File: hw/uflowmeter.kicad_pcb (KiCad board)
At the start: 4 copper layers, 70 x 55 mm, 54 parts, among them J1 SBW, J2 ANT, J3 Display, J4 Transducers, J5 Cal UART, Q1 IRLML6401, SW1 Button, U1 MSP430FR5043IRGC, U2 CC1101RGPR, Y1 32.768kHz, Y2 8MHz, Y3 26MHz

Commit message: hw: fabrication export, fiducials, and an honest account of what is left
make_fab.sh writes the JLCPCB set from the board file: the four copper
layers, both masks, silkscreens and paste layers, the outline and both drill
files, zipped, plus the BOM and the placement CSV in the column names the
assembly step wants. It caught its own bug on the first run -- KiCad names
Gerbers by layer, .gtl .gbl .g1 .g2 and so on, so a wildcard on .gbr ships an
archive containing nothing but drill files.

finish_board.py adds what a router will not: three fiducials in an asymmetric
L, because a QFN-64 on 0.5 mm pitch is placed from fiducials rather than from
the board outline, and a legend on both sides.

The board is NOT orderable, and the docs now say so plainly. 32 connections
are missing. Fifteen are the RF chain: route_rf.py manages two hops of
eighteen because the shunt parts sit across the straight line between the
series ones, and making room means choosing a geometry, which is the one
thing that must not be chosen freely -- TI's values are only correct with
TI's layout. That layout is in the SWRR045 archive as CADSTAR and Gerbers,
readable by a person and not by a script.

The other seventeen are signals on fifteen nets, almost all the last pins of
the two QFNs where the room runs out. They want a router that can push what
is already laid; mine only add.

Three dead ends are recorded so nobody repeats them: reordering the nets (six
orderings, the one in use was best, and hardest-first scored worst),
unbounding the search (12 mm to 30 mm margin changed the result by exactly
nothing), and running further passes (identical output plus duplicate
copper). What is left is congestion, and congestion wants rip-up.

Co-Authored-By: Claude Opus 5 (1M context) <noreply@anthropic.com>
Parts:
- added FID1: , Fiducial_1mm_Mask2mm, F.Cu at (3.45, 3.45)
- added FID2: , Fiducial_1mm_Mask2mm, F.Cu at (66.5, 3.45)
- added FID3: , Fiducial_1mm_Mask2mm, F.Cu at (3.45, 51.5)
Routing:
- net RFE: track 0.00 -> 4.00 mm
- net RFC: track 0.00 -> 3.00 mm
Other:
- board text added: "uflowmeter rev A"

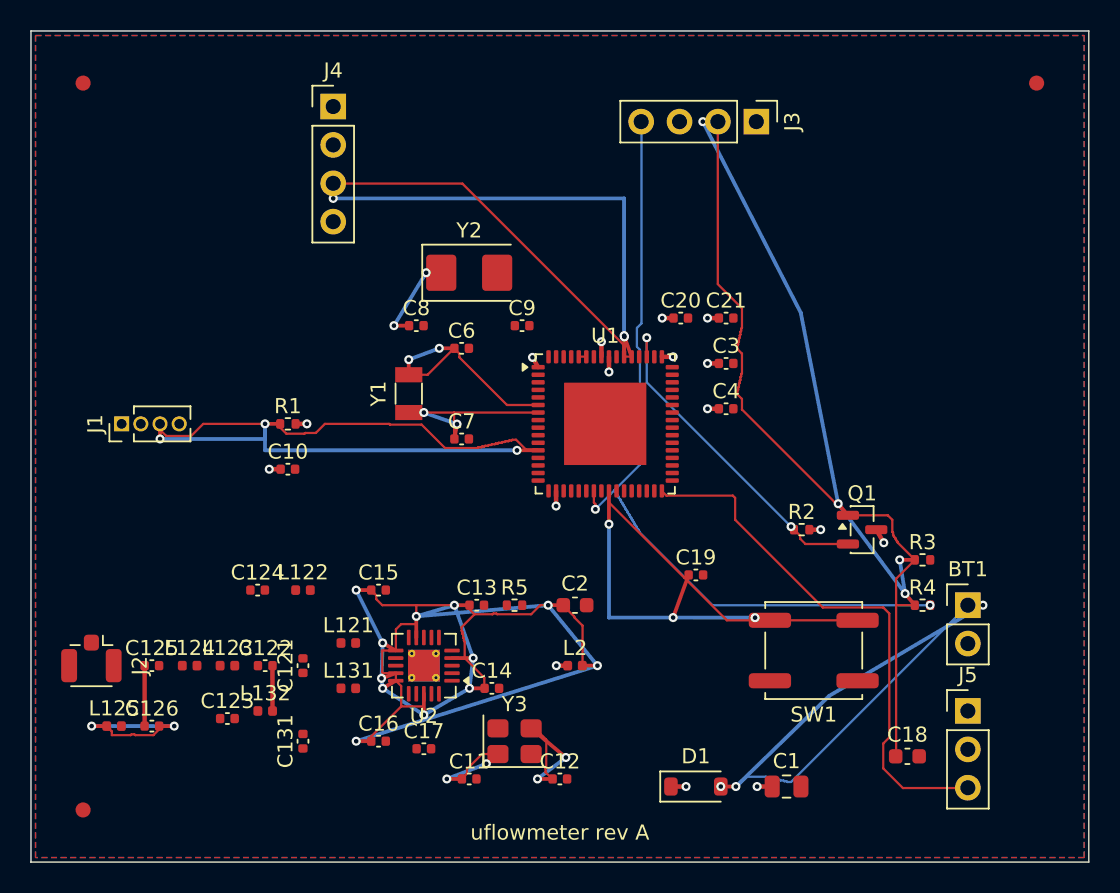
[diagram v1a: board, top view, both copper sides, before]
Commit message: hw: the radio becomes a module, and a real schematic that caught a real bug
The CC1101 is no longer on this board. Gone with it: its 26 MHz crystal, its
bias resistor, its supply bead and decoupling, the whole filter balun and the
notch, and the u.FL connector -- twenty parts. J6 carries eight pins to a
ready-made module instead, and the firmware did not change by a line.

That removed the two hardest problems in the design. TI's reference layout no
longer has to be transplanted, which mattered because it exists only as
CADSTAR and Gerbers -- readable by a person, not by a script. And EN 300 220
no longer has to be proven by conducted measurement, which an antenna
connector on your own board obliges you to do.

What the module must be is now in RF.md, and the third condition is the one
that quietly ruins a battery meter: no power LED. An indicator LED is a
milliamp against this instrument's 5.7 uA, two hundred times the whole thing.

uflowmeter.kicad_sch is generated from the netlist with every symbol drawn in
the file, so it opens the same anywhere. It is verified the only way that
proves anything: export the netlist back out of it and compare. The first run
disagreed on RST -- and it was not the generator that was wrong. C10 pin 1 was
declared on both VCC and RST. It is the reset capacitor; its plate belongs to
RST alone. mknet.py now refuses to emit a netlist where two nets claim one
pad.

The board that comes out of all this is 29 components and 22 nets, down from
54 and 37. Routing went from 34 unconnected to 6, DRC clean. build_board.sh
runs the whole path from the netlist source to the fabrication files.

Co-Authored-By: Claude Opus 5 (1M context) <noreply@anthropic.com>
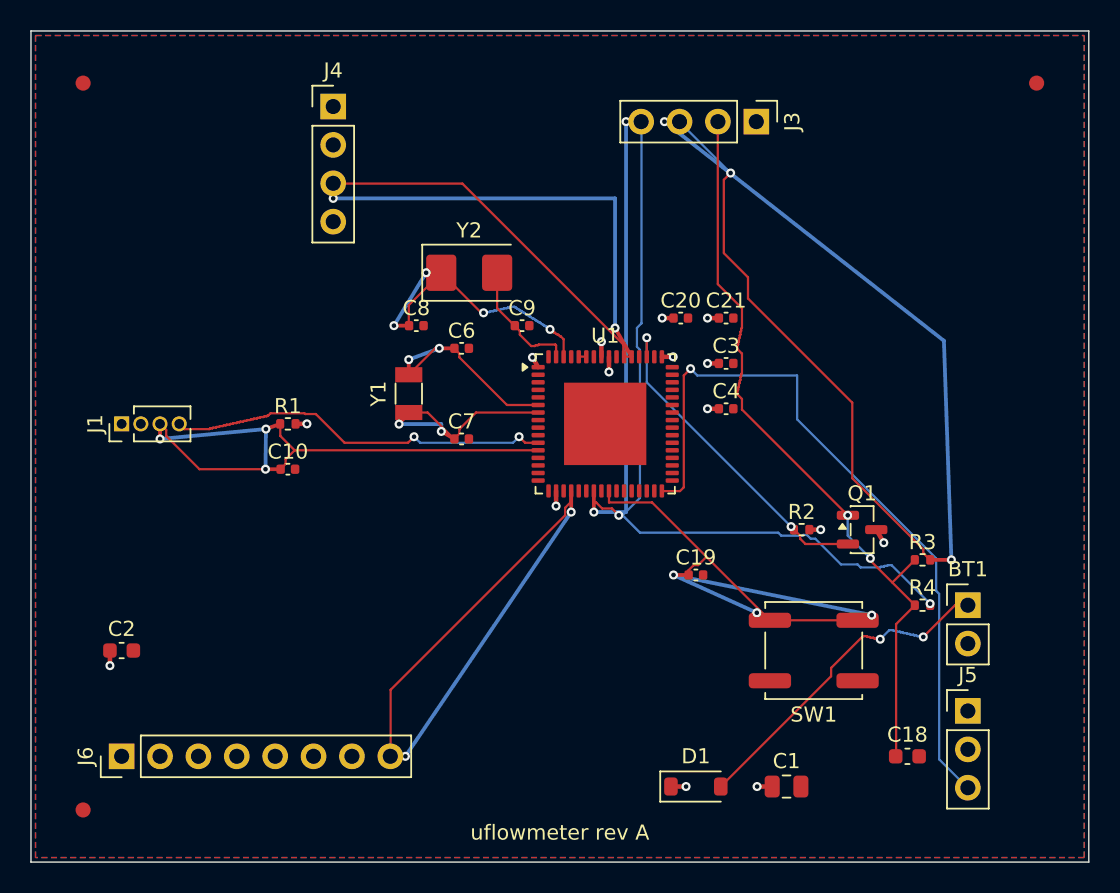
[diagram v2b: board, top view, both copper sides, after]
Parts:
- removed C11, C125: 12pF, C_0402_1005Metric
- removed C12: 15pF, C_0402_1005Metric
- removed C121: 1.0pF, C_0402_1005Metric
- removed C122, C131: 1.5pF, C_0402_1005Metric
- removed C123: 3.3pF, C_0402_1005Metric
- removed C124: 100pF, C_0402_1005Metric
- removed C126: 47pF, C_0402_1005Metric
- removed C13, C14, C15, C16, C17: 100nF, C_0402_1005Metric
- removed J2: ANT, U.FL_Hirose_U.FL-R-SMT-1_Vertical
- removed L121, L123, L124, L131: 12nH, L_0402_1005Metric
- removed L122, L132: 18nH, L_0402_1005Metric
- removed L125: 3.3nH, L_0402_1005Metric
- removed L2: FerriteBead, L_0402_1005Metric
- removed R5: 56k, R_0402_1005Metric
- removed U2: CC1101RGPR, TQFN-20-1EP_4x4mm_P0.5mm_EP2.1x2.1mm_ThermalVias
- removed Y3: 26MHz, Crystal_SMD_3225-4Pin_3.2x2.5mm
- added J6: Radio module, PinHeader_1x08_P2.54mm_Vertical, F.Cu at (6.00, 48.0)
- moved C2 30.1 mm to (6.00, 41.0)
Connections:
- C10 pad 1: VCC -> RST
- C2 pad 1: RADIO_VDD -> VCC
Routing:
- net RADIO_VDD: track 105.5 -> 0.00 mm, vias 12 -> 0
- net I2C_SCL: track 0.00 -> 76.4 mm, vias 0 -> 3
- net SPI_MISO: track 0.00 -> 43.9 mm, vias 0 -> 2
- net VCC_DISP: track 91.2 -> 49.8 mm, vias 4 -> 2
- net I2C_SDA: track 52.8 -> 82.8 mm, vias 2 -> 4
- net TEST: track 0.00 -> 25.6 mm, vias 0 -> 2
- net BAT+: track 43.9 -> 21.9 mm, vias 3 -> 2
- net RST: track 56.8 -> 41.4 mm
- net USSXTIN: track 6.10 -> 21.4 mm, vias 2 -> 4
- net UART_RX: track 35.6 -> 48.6 mm, vias 0 -> 1
- net RFNOTCH: track 11.5 -> 0.00 mm, vias 2 -> 0
- net XOSC_Q2: track 10.2 -> 0.00 mm, vias 2 -> 0
- net XOSC_Q1: track 7.82 -> 0.00 mm, vias 2 -> 0
- net USSXTOUT: track 0.00 -> 7.76 mm
- net RFE: track 4.00 -> 0.00 mm
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
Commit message: hw: the board is routed -- zero violations, zero unconnected
32 footprints, 222 tracks, 89 vias on 70.1 x 55.1 mm of four-layer board.
DRC clean, ERC clean, and fab/ holds the Gerbers, both drill files, the BOM
and the placement list.

The last connections came in once one rule was written down. A 0.6 mm via
needs 0.525 mm of clear board to a foreign track -- its own radius, plus the
clearance, plus the other track's half width -- and escapes from adjacent
pins of a 0.5 mm pitch package run 0.5 mm apart. That is always a hair too
close, so a via never goes directly behind a pin: one of each adjacent pair
fans sideways first. That was needed four times, for I2C_SCL/BUTTON,
DISP_GATE/RADIO_CS, UART_TX/UART_RX and USSXTIN/USSXTOUT.

The nets the grid router could not reach are in route_by_hand.py as explicit
waypoints under a discipline that makes crossings impossible rather than
unlikely: verticals on the top layer, horizontals on the bottom, a via at
every corner, a lane of its own for each net. Drawn by eye instead, the same
routes produced seven crossings.

Three other things had to be fixed along the way. The supply stitcher was
testing candidate vias against pads only, not against copper already on the
board, so it dropped them onto hand-laid tracks. DISP_GATE's fan passed over
DVCC3 and kept that pin's stub in violation, so the pin was left orphaned
every build. And routing boxed a 12 mm2 patch of ground in above U1 which
held a pad, so island removal kept it while nothing on its own layer reached
it -- one via ties it to the plane.

Ordering it is not the same as it working. Nothing has been near a
transducer, a pipe or a battery; what sits between CH0/CH1 and the
transducers is still undesigned; and the radio module has three conditions to
meet.

Co-Authored-By: Claude Opus 5 (1M context) <noreply@anthropic.com>
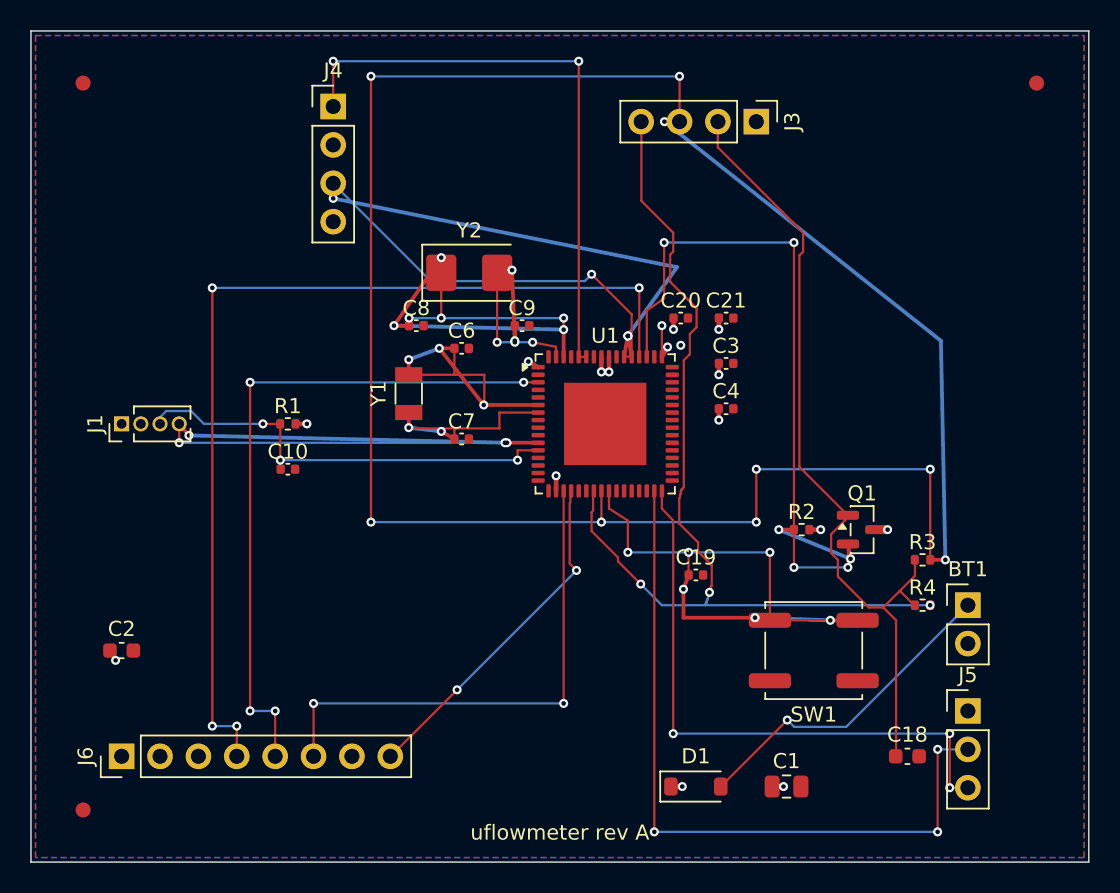
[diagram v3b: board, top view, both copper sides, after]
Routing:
- net RADIO_CS: track 0.00 -> 65.4 mm, vias 0 -> 4
- net I2C_SCL: track 76.4 -> 141.3 mm, vias 3 -> 9
- net UART_TX: track 0.00 -> 48.8 mm, vias 0 -> 3
- net SPI_SCK: track 0.00 -> 45.5 mm, vias 0 -> 4
- net CH0: track 0.30 -> 39.3 mm, vias 0 -> 2
- net SPI_MOSI: track 0.00 -> 34.1 mm, vias 0 -> 2
- net DISP_GATE: track 21.6 -> 50.5 mm, vias 2 -> 6
- net TEST: track 25.6 -> 49.1 mm, vias 2 -> 4
- net SPI_MISO: track 43.9 -> 22.2 mm
- net I2C_SDA: track 82.8 -> 62.3 mm, vias 4 -> 3
- net USSXTIN: track 21.4 -> 36.8 mm, vias 4 -> 6
- net RST: track 41.4 -> 29.4 mm
- net LFXIN: track 14.6 -> 24.8 mm, vias 2 -> 3
- net USSXTOUT: track 7.76 -> 17.0 mm, vias 0 -> 5
- net UART_RX: track 48.6 -> 39.4 mm, vias 1 -> 3
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
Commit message: hw: a switch the assembly house actually stocks
SW1 was a CK KSC7xx, which has no stocked equivalent, so the button came back
as an unmatched component and would never have been placed. It is now an ALPS
SKQGADE010 -- C116647, 88,965 in stock -- for which KiCad already carries a
checked footprint, so nothing had to be drawn from a description.

The swap moved its pad by 0.2 mm and taught two things.

Its footprint carries a keepout on the top layer, and rightly: there is a
metal dome under the button and copper there would short against it. BAT+ ran
straight through it. The keepout binds only the top layer, so BAT+ now passes
underneath on the bottom and comes up west of the switch.

And RST had never actually reached the debug header -- the maze router had
been quietly covering that, and stopped once the board around it changed. It
cannot run along y=26 on the top layer because J1's TEST pin is in the way,
so it carries on west underneath and surfaces outside the connector.

23 parts are machine-placed now. What is left by hand is six through-hole
headers, which no SMT service places anyway and which are the easiest things
on the board to solder.

Zero DRC violations, zero unconnected, ERC clean.

Co-Authored-By: Claude Opus 5 (1M context) <noreply@anthropic.com>
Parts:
- SW1: footprint SW_Push_1P1T_NO_CK_KSC7xxJ -> SW_SPST_SKQG_WithoutStem
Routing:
- net RST: track 29.4 -> 46.1 mm, vias 3 -> 6
- net BUTTON: track 41.2 -> 26.1 mm, vias 6 -> 3
- net BAT+: track 21.4 -> 28.4 mm
- net USSXTOUT: track 17.0 -> 10.3 mm, vias 5 -> 3
- net VCC_DISP: track 53.3 -> 48.9 mm
- net USSXTIN: track 36.8 -> 32.9 mm
- net I2C_SDA: track 62.3 -> 63.6 mm
- net TEST: track 49.1 -> 50.0 mm
- net DISP_GATE: track 50.5 -> 49.7 mm

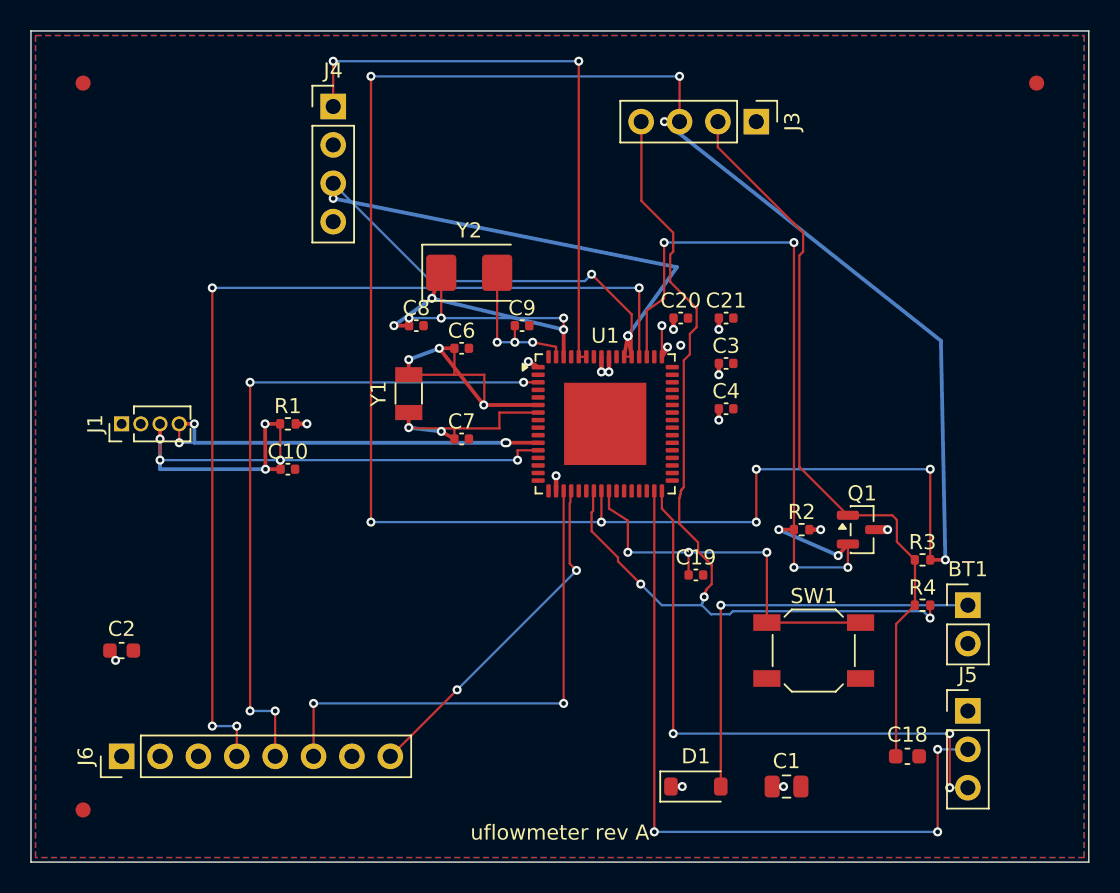
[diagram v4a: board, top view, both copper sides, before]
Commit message: hw: two nets were routed twice, and nothing was watching for it
CH1 carried 59 mm of copper and four vias where one path does; USSXTIN and
LFXIN each had a complete second route laid beside the first. Both routing
passes took every net rather than only the unfinished ones, so the second
pass rebuilt work the first had already done.

DRC cannot see this. Both paths are on the same net, so nothing shorts and
nothing is unconnected -- the board reported zero violations and zero
unconnected while carrying copper nobody asked for. Watching those two
numbers, which is all this project had been doing, is blind to it.

The first attempt at a guard was worse than none. GetRatsnestForNet hands
back an opaque object with no length, so len(...) == 0 raises TypeError, and
the try/except around it reported every net as unfinished. It guarded
nothing, and the only reason that surfaced was CH1 growing again on the next
build. Both routers now ask DRC and read the net names out of its unconnected
list.

audit_nets.py is the check that was missing: each net's track length against
the minimum spanning tree over its pads, which is the floor for any routing
of it. Lane-routed nets sit at 1.5-2.5x because the Manhattan discipline is
deliberately not shortest; a ratio of three is a second path.

CH1 is now routed by hand like CH0 -- the two adjacent pins tied at the
package, one path out, and J4.3 approached from the side because coming
straight down x=20 crosses the ground pin above it.

347 tracks, 72 vias. Zero DRC violations, zero unconnected, ERC clean, and
nothing over 2.5x its floor.

Co-Authored-By: Claude Opus 5 (1M context) <noreply@anthropic.com>
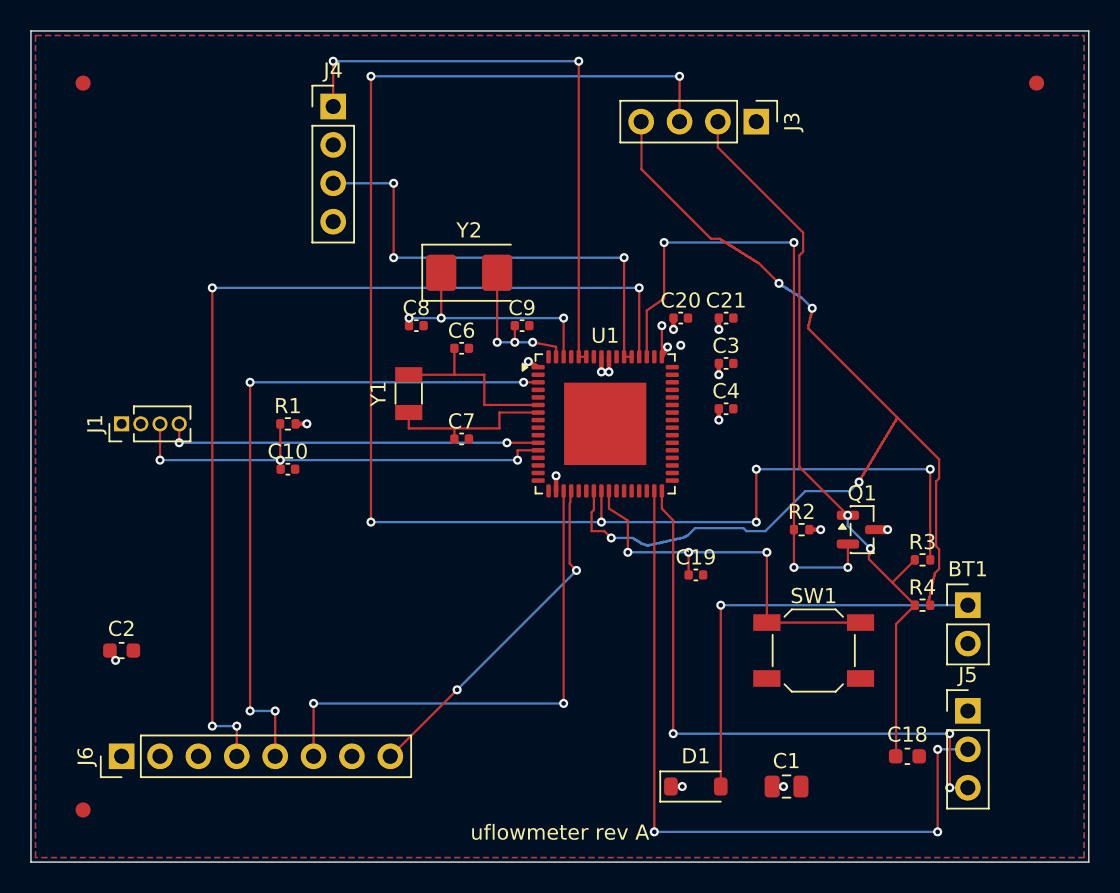
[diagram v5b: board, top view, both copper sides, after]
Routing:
- net I2C_SCL: track 141.3 -> 101.5 mm, vias 9 -> 7
- net CH1: track 59.2 -> 31.2 mm, vias 4 -> 3
- net TEST: track 50.0 -> 25.0 mm, vias 4 -> 2
- net USSXTIN: track 32.9 -> 16.3 mm, vias 6 -> 3
- net RST: track 46.1 -> 31.1 mm, vias 6 -> 3
- net LFXIN: track 24.8 -> 12.3 mm, vias 3 -> 0
- net DISP_GATE: track 49.7 -> 43.4 mm, vias 6 -> 4
- net I2C_SDA: track 63.6 -> 69.8 mm, vias 3 -> 4
- net LFXOUT: track 15.5 -> 11.4 mm, vias 2 -> 0
- net VCC_DISP: track 48.9 -> 49.6 mm, vias 0 -> 2
